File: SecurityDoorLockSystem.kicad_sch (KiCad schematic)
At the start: 12 parts, among them J1 Power In, J2 Servo, J3 RFID-RC522, J4 R307s, U1 ESP32-DEVKIT-V1, U2 L7805

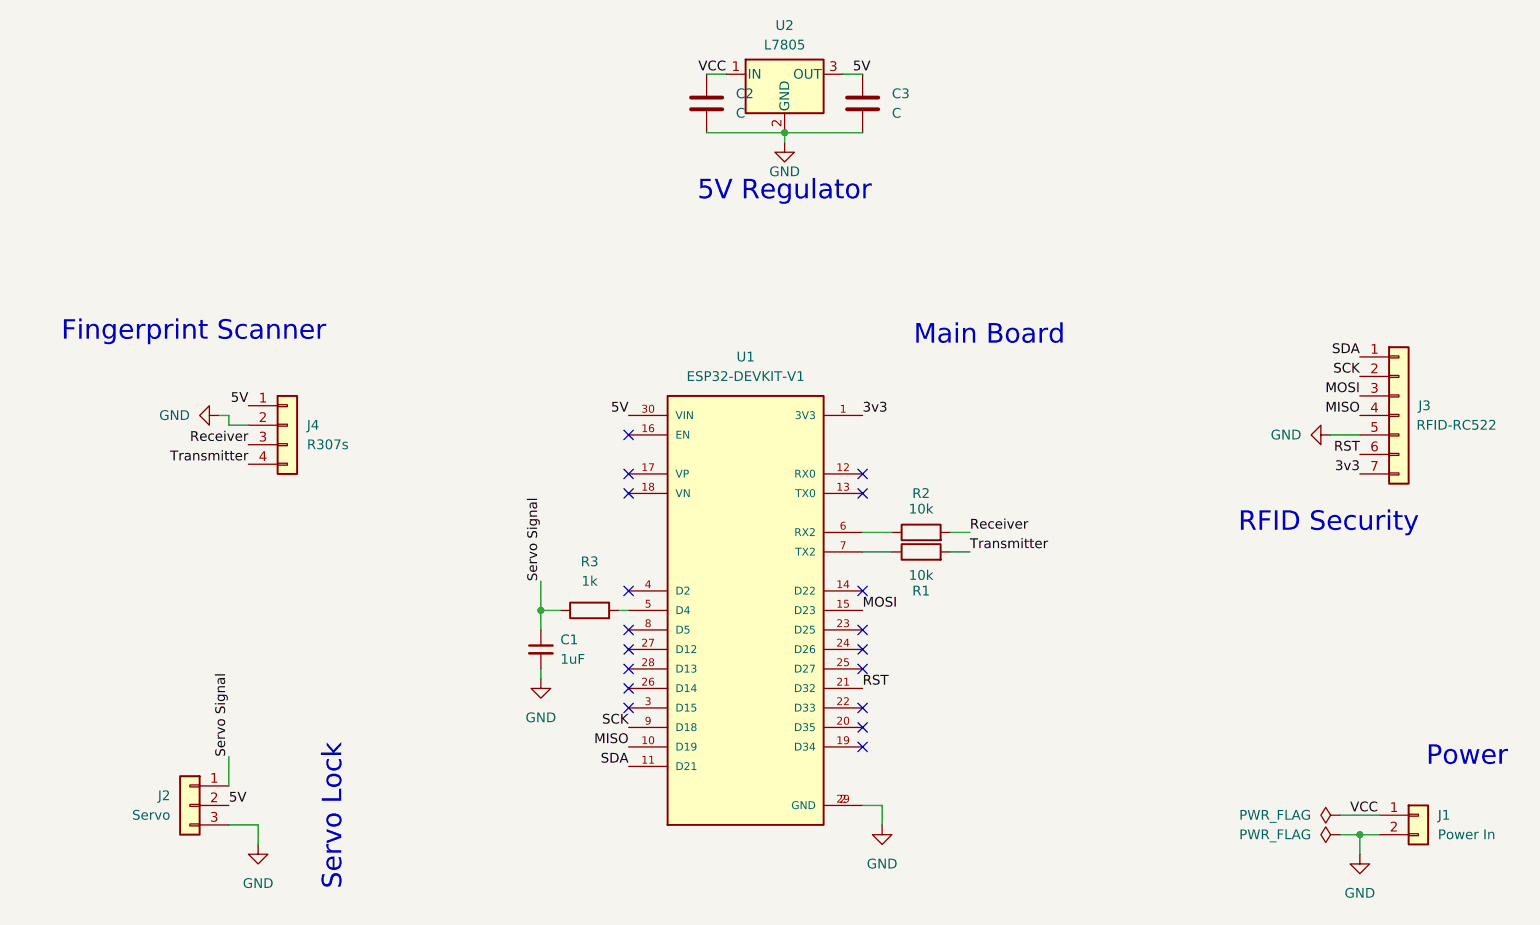
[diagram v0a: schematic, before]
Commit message: added: protection -- modified: pcb, schematic
added power source polarity protection
changed tracks (sizes and routes)
changed schematic diagram connectors to screw terminals
changed pcb connectors to screw terminals
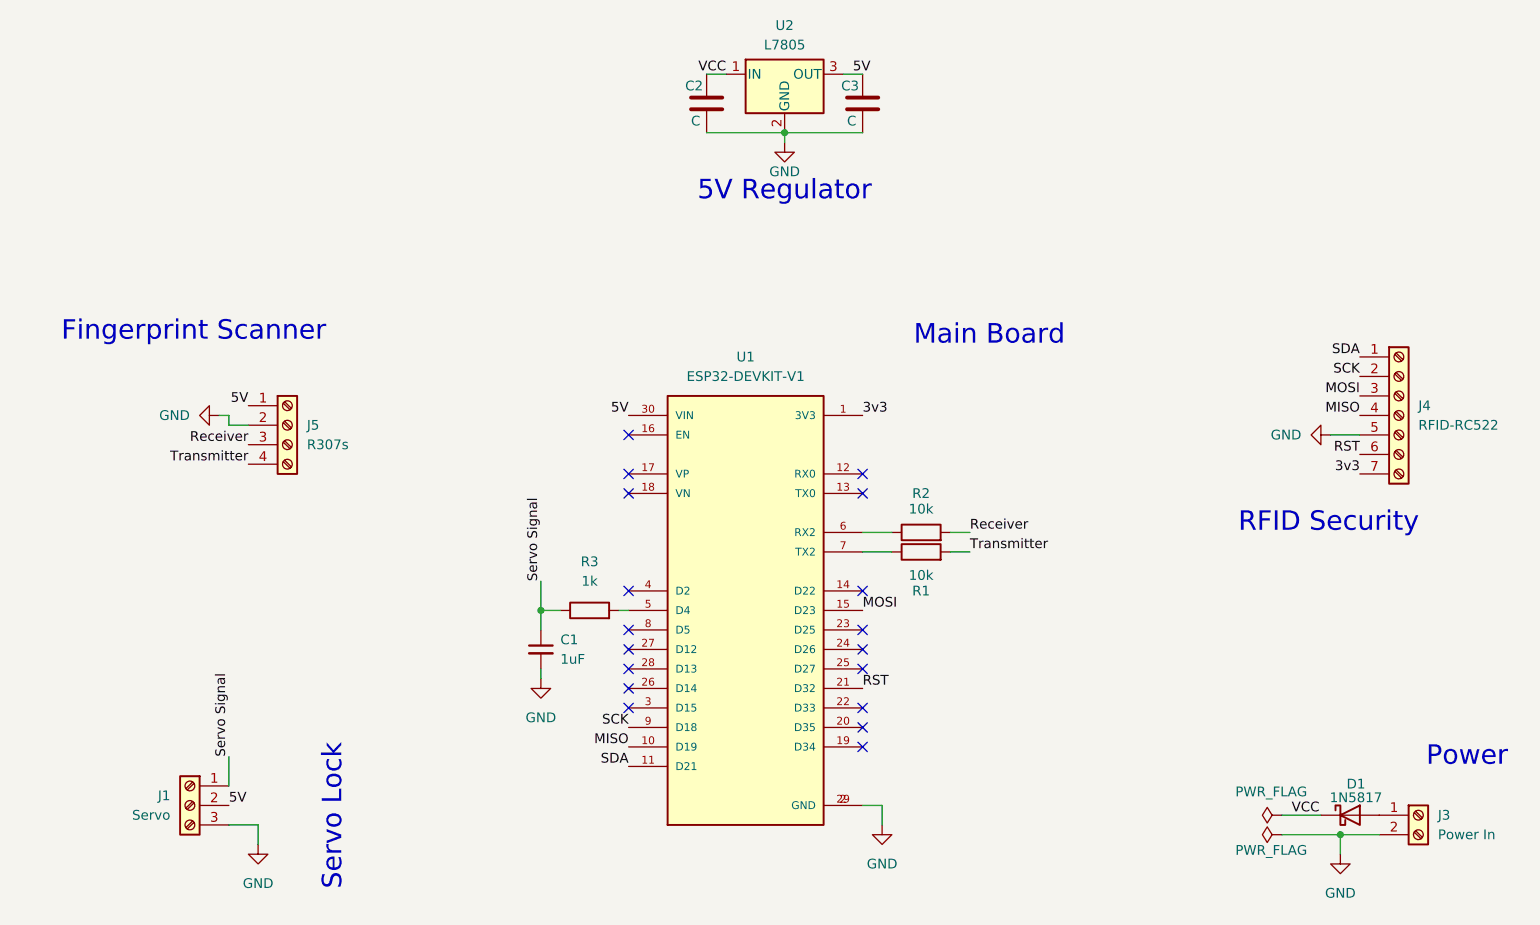
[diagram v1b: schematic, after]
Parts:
- removed J1: Power In, TerminalBlock_CUI:TerminalBlock_CUI_TB007-508-02_1x02_P5.08mm_Horizontal, symbol Connector_Generic:Conn_01x02
- removed J2: Servo, TerminalBlock_CUI:TerminalBlock_CUI_TB007-508-03_1x03_P5.08mm_Horizontal, symbol Connector_Generic:Conn_01x03
- removed J3: RFID-RC522, TerminalBlock_CUI:TerminalBlock_CUI_TB007-508-07_1x07_P5.08mm_Horizontal, symbol Connector_Generic:Conn_01x07
- removed J4: R307s, TerminalBlock_CUI:TerminalBlock_CUI_TB007-508-04_1x04_P5.08mm_Horizontal, symbol Connector_Generic:Conn_01x04
- added D1: 1N5817, Diode_THT:D_DO-41_SOD81_P7.62mm_Horizontal, symbol Diode:1N5817
- added J1: Servo, TerminalBlock_Phoenix:TerminalBlock_Phoenix_MKDS-1,5-3_1x03_P5.00mm_Horizontal, symbol Connector:Screw_Terminal_01x03
- added J3: Power In, TerminalBlock_Phoenix:TerminalBlock_Phoenix_MKDS-1,5-2_1x02_P5.00mm_Horizontal, symbol Connector:Screw_Terminal_01x02
- added J4: RFID-RC522, TerminalBlock_Phoenix:TerminalBlock_Phoenix_MKDS-1,5-7_1x07_P5.00mm_Horizontal, symbol Connector:Screw_Terminal_01x07
- added J5: R307s, TerminalBlock_Phoenix:TerminalBlock_Phoenix_MKDS-1,5-4_1x04_P5.00mm_Horizontal, symbol Connector:Screw_Terminal_01x04
- C3: footprint (none) -> Capacitor_THT:C_Radial_D5.0mm_H7.0mm_P2.00mm
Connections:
- net 3v3: now also J4.7 (Pin_7)
- net 5V: now also J1.2 (Pin_2), J5.1 (Pin_1)
- net GND: now also J1.3 (Pin_3), J3.2 (Pin_2), J4.5 (Pin_5), J5.2 (Pin_2)
- net MISO: now also J4.4 (Pin_4)
- net MOSI: now also J4.3 (Pin_3)
- net RST: now also J4.6 (Pin_6)
- net Receiver: now also J5.3 (Pin_3)
- net SCK: now also J4.2 (Pin_2)
- net SDA: now also J4.1 (Pin_1)
- net Servo Signal: now also J1.1 (Pin_1)
- net Transmitter: now also J5.4 (Pin_4)
- net VCC: now also D1.1 (K)
- new net: D1.2 (A), J3.1 (Pin_1)

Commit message: modified capacitor values
changed value of capacitors 1 and 2; C1 = 100uF, C2 = 50uF
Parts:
- C1: renamed from C2; value C -> 150uF
- C2: renamed from C3; value C -> 50uF
- renumbered C1 to C3, J4 to J1, J5 to J2, J1 to J3, J3 to J4, R2 to R1, R1 to R2, U2 to U1, U1 to U2
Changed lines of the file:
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@@
-		(polyline
-			(pts
-				(xy 125.73 33.02) (xy 125.73 59.69) (xy 160.02 59.69) (xy 160.02 33.02)
-			)
-			(stroke
-				(width 0)
-				(type dash)
-			)
-			(fill
-				(type none)
-			)
-		)
-	)
-	(rule_area
 		(polyline
 			(pts
@@
 		(polyline
 			(pts
-				(xy 104.14 72.39) (xy 180.34 72.39) (xy 180.34 151.13) (xy 104.14 151.13)
+				(xy 123.19 33.02) (xy 157.48 33.02) (xy 157.48 59.69) (xy 123.19 59.69)
 			)
 			(stroke
@@
 		)
 	)
+	(rule_area
+		(polyline
+			(pts
+				(xy 104.14 72.39) (xy 180.34 72.39) (xy 180.34 151.13) (xy 104.14 151.13)
+			)
+			(stroke
+				(width 0)
+				(type dash)
+			)
+			(fill
+				(type none)
+			)
+		)
+	)
 	(symbol
 		(lib_id "power:PWR_FLAG")
@@
 		(on_board yes)
 		(dnp no)
-		(property "Reference" "J1"
+		(property "Reference" "J3"
 			(at 60.96 135.8899 0)
 			(effects
@@
 			(project ""
 				(path "/8711d31f-b08a-48db-983d-0d74003b609c"
-					(reference "J1")
+					(reference "J3")
 					(unit 1)
 				)
@@
 		(dnp no)
 		(fields_autoplaced yes)
-		(property "Reference" "#PWR05"
+		(property "Reference" "#PWR04"
 			(at 109.22 127 0)
 			(effects
@@
 			(project "SecurityDoorLockSystem"
 				(path "/8711d31f-b08a-48db-983d-0d74003b609c"
-					(reference "#PWR05")
+					(reference "#PWR04")
 					(unit 1)
 				)
@@
 		(dnp no)
 		(fields_autoplaced yes)
-		(property "Reference" "#PWR09"
+		(property "Reference" "#PWR02"
 			(at 60.96 86.36 0)
 			(effects
@@
 			(project ""
 				(path "/8711d31f-b08a-48db-983d-0d74003b609c"
-					(reference "#PWR09")
+					(reference "#PWR02")
 					(unit 1)
 				)
@@
 		(on_board yes)
 		(dnp no)
-		(property "Reference" "R1"
+		(property "Reference" "R2"
 			(at 158.75 109.22 90)
 			(effects
@@
 			(project ""
 				(path "/8711d31f-b08a-48db-983d-0d74003b609c"
-					(reference "R1")
+					(reference "R2")
 					(unit 1)
 				)
@@
 		(dnp no)
 		(fields_autoplaced yes)
-		(property "Reference" "U2"
+		(property "Reference" "U1"
 			(at 140.97 35.56 0)
 			(effects
@@
 			(project ""
 				(path "/8711d31f-b08a-48db-983d-0d74003b609c"
-					(reference "U2")
+					(reference "U1")
 					(unit 1)
 				)
@@
 		(dnp no)
 		(fields_autoplaced yes)
-		(property "Reference" "J4"
+		(property "Reference" "J1"
 			(at 223.52 85.0899 0)
 			(effects
@@
 			(project ""
 				(path "/8711d31f-b08a-48db-983d-0d74003b609c"
-					(reference "J4")
+					(reference "J1")
 					(unit 1)
 				)
@@
 		(on_board yes)
 		(dnp no)
-		(property "Reference" "#PWR07"
+		(property "Reference" "#PWR01"
 			(at 140.97 57.15 0)
 			(effects
@@
 			(project ""
 				(path "/8711d31f-b08a-48db-983d-0d74003b609c"
-					(reference "#PWR07")
+					(reference "#PWR01")
 					(unit 1)
 				)
@@
 		(on_board yes)
 		(dnp no)
-		(property "Reference" "C3"
-			(at 148.336 43.434 0)
+		(property "Reference" "C2"
+			(at 151.384 43.434 0)
 			(effects
 				(font
@@
 			)
 		)
-		(property "Value" "C"
-			(at 149.098 48.006 0)
+		(property "Value" "50uF"
+			(at 151.638 48.006 0)
 			(effects
 				(font
@@
 			(project "SecurityDoorLockSystem"
 				(path "/8711d31f-b08a-48db-983d-0d74003b609c"
-					(reference "C3")
+					(reference "C2")
 					(unit 1)
 				)
@@
 		(dnp no)
 		(fields_autoplaced yes)
-		(property "Reference" "J5"
+		(property "Reference" "J2"
 			(at 78.74 87.6299 0)
 			(effects
@@
 			(project ""
 				(path "/8711d31f-b08a-48db-983d-0d74003b609c"
-					(reference "J5")
+					(reference "J2")
 					(unit 1)
 				)
@@
 		(dnp no)
 		(fields_autoplaced yes)
-		(property "Reference" "#PWR012"
+		(property "Reference" "#PWR03"
 			(at 205.74 88.9 0)
 			(effects
@@
 			(project ""
 				(path "/8711d31f-b08a-48db-983d-0d74003b609c"
-					(reference "#PWR012")
+					(reference "#PWR03")
 					(unit 1)
 				)
@@
 		(dnp no)
 		(fields_autoplaced yes)
-		(property "Reference" "U1"
+		(property "Reference" "U2"
 			(at 135.89 78.74 0)
 			(effects
@@
 			(project ""
 				(path "/8711d31f-b08a-48db-983d-0d74003b609c"
-					(reference "U1")
+					(reference "U2")
 					(unit 1)
 				)
@@
 		(on_board yes)
 		(dnp no)
-		(property "Reference" "R2"
+		(property "Reference" "R1"
 			(at 158.75 96.52 90)
 			(effects
@@
 			(project ""
 				(path "/8711d31f-b08a-48db-983d-0d74003b609c"
-					(reference "R2")
+					(reference "R1")
 					(unit 1)
 				)
@@
 		(dnp no)
 		(fields_autoplaced yes)
-		(property "Reference" "#PWR06"
+		(property "Reference" "#PWR07"
 			(at 213.36 149.86 0)
 			(effects
@@
 			(project ""
 				(path "/8711d31f-b08a-48db-983d-0d74003b609c"
-					(reference "#PWR06")
+					(reference "#PWR07")
 					(unit 1)
 				)
@@
 		(dnp no)
 		(fields_autoplaced yes)
-		(property "Reference" "C1"
+		(property "Reference" "C3"
 			(at 111.76 115.5762 0)
 			(effects
@@
 			(project ""
 				(path "/8711d31f-b08a-48db-983d-0d74003b609c"
-					(reference "C1")
+					(reference "C3")
 					(unit 1)
 				)
@@
 		(dnp no)
 		(fields_autoplaced yes)
-		(property "Reference" "#PWR03"
+		(property "Reference" "#PWR06"
 			(at 72.39 148.59 0)
 			(effects
@@
 			(project ""
 				(path "/8711d31f-b08a-48db-983d-0d74003b609c"
-					(reference "#PWR03")
+					(reference "#PWR06")
 					(unit 1)
 				)
@@
 		(dnp no)
 		(fields_autoplaced yes)
-		(property "Reference" "J3"
+		(property "Reference" "J4"
 			(at 226.06 138.4299 0)
 			(effects
@@
 			(project ""
 				(path "/8711d31f-b08a-48db-983d-0d74003b609c"
-					(reference "J3")
+					(reference "J4")
 					(unit 1)
 				)
@@
 		(dnp no)
 		(fields_autoplaced yes)
-		(property "Reference" "#PWR02"
+		(property "Reference" "#PWR05"
 			(at 153.67 146.05 0)
 			(effects
@@
 			(project ""
 				(path "/8711d31f-b08a-48db-983d-0d74003b609c"
-					(reference "#PWR02")
+					(reference "#PWR05")
 					(unit 1)
 				)
@@
 		(on_board yes)
 		(dnp no)
-		(property "Reference" "C2"
+		(property "Reference" "C1"
 			(at 128.016 43.434 0)
 			(effects
@@
 			)
 		)
-		(property "Value" "C"
-			(at 128.778 48.006 0)
+		(property "Value" "150uF"
+			(at 124.714 48.006 0)
 			(effects
 				(font
@@
 			(project ""
 				(path "/8711d31f-b08a-48db-983d-0d74003b609c"
-					(reference "C2")
-					(unit 1)
-				)
+					(reference "C1")
+					(unit 1)
+				)

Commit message: added lcd
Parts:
- added J5: LCD Conn, TerminalBlock_Phoenix:TerminalBlock_Phoenix_MKDS-1,5-4_1x04_P5.00mm_Horizontal, symbol Connector:Screw_Terminal_01x04
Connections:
- net 5V: now also J5.2 (Pin_2)
- net GND: now also J5.1 (Pin_1)
- net SDA: now also J5.4 (Pin_4); no longer J1.1 (Pin_1)
- net Rx: now reaches U2.12 (RX0)
- net Rx: now also J1.1 (Pin_1)
- net Tx: now reaches U2.13 (TX0)
- net Tx: now also J1.4 (Pin_4)
- net SCL: now reaches U2.14 (D22)
- net SCL: now also J5.3 (Pin_3)
- net MISO: no longer names the net of U2.10 (D19)
- net MISO: no longer J1.4 (Pin_4)
- no-connect marks 18 -> 16
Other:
- note added: "Display"
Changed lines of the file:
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@@
+		)
+	)
+	(text "Display\n"
+		(exclude_from_sim no)
+		(at 213.868 56.134 0)
+		(effects
+			(font
+				(size 2.54 2.54)
+			)
 		)
 	)
@@
 	)
 	(no_connect
-		(at 151.13 109.22)
-	)
-	(no_connect
 		(at 151.13 116.84)
 	)
@@
 	)
 	(no_connect
-		(at 151.13 96.52)
-	)
-	(no_connect
 		(at 120.65 96.52)
 	)
@@
 	)
 	(no_connect
+		(at 120.65 129.54)
+	)
+	(no_connect
 		(at 120.65 124.46)
 	)
@@
 		(at 120.65 119.38)
 	)
-	(no_connect
-		(at 151.13 93.98)
-	)
 	(wire
 		(pts
@@
 		(pts
 			(xy 213.36 143.51) (xy 213.36 140.97)
+		)
+		(stroke
+			(width 0)
+			(type default)
+		)
+	)
+	(wire
+		(pts
+			(xy 203.2 44.45) (xy 209.55 44.45)
 		)
 		(stroke
@@
 		)
 	)
+	(label "Rx"
+		(at 151.13 93.98 0)
+		(effects
+			(font
+				(size 1.27 1.27)
+			)
+			(justify left bottom)
+		)
+	)
 	(label "RST"
 		(at 151.13 121.92 0)
@@
 		)
 	)
+	(label "5V"
+		(at 209.55 46.99 180)
+		(effects
+			(font
+				(size 1.27 1.27)
+			)
+			(justify right bottom)
+		)
+	)
 	(label "SDA"
 		(at 120.65 132.08 180)
@@
 		)
 	)
-	(label "SDA"
+	(label "Rx"
 		(at 215.9 78.74 180)
 		(effects
@@
 		)
 	)
+	(label "SDA"
+		(at 209.55 52.07 180)
+		(effects
+			(font
+				(size 1.27 1.27)
+			)
+			(justify right bottom)
+		)
+	)
 	(label "VCC"
 		(at 133.35 41.91 180)
@@
 		)
 	)
-	(label "MISO"
+	(label "Tx"
 		(at 215.9 86.36 180)
 		(effects
@@
 		)
 	)
+	(label "SCL"
+		(at 151.13 109.22 0)
+		(effects
+			(font
+				(size 1.27 1.27)
+			)
+			(justify left bottom)
+		)
+	)
 	(label "3v3"
 		(at 151.13 86.36 0)
@@
 		)
 	)
+	(label "Tx"
+		(at 151.13 96.52 0)
+		(effects
+			(font
+				(size 1.27 1.27)
+			)
+			(justify left bottom)
+		)
+	)
 	(label "3v3"
 		(at 215.9 93.98 180)
@@
 		)
 	)
-	(label "MISO"
-		(at 120.65 129.54 180)
+	(label "SCL"
+		(at 209.55 49.53 180)
 		(effects
 			(font
@@
 			(pts
 				(xy 53.34 111.76) (xy 53.34 151.13) (xy 86.36 151.13) (xy 86.36 111.76)
+			)
+			(stroke
+				(width 0)
+				(type dash)
+			)
+			(fill
+				(type none)
+			)
+		)
+	)
+	(rule_area
+		(polyline
+			(pts
+				(xy 200.66 41.91) (xy 200.66 58.42) (xy 227.33 58.42) (xy 227.33 41.91)
 			)
 			(stroke
@@
 	)
 	(symbol
+		(lib_id "power:GND")
+		(at 203.2 44.45 0)
+		(unit 1)
+		(exclude_from_sim no)
+		(in_bom yes)
+		(on_board yes)
+		(dnp no)
+		(fields_autoplaced yes)
+		(property "Reference" "#PWR08"
+			(at 203.2 50.8 0)
+			(effects
+				(font
+					(size 1.27 1.27)
+				)
+				(hide yes)
+			)
+		)
+		(property "Value" "GND"
+			(at 203.2 49.53 0)
+			(effects
+				(font
+					(size 1.27 1.27)
+				)
+			)
+		)
+		(property "Footprint" ""
+			(at 203.2 44.45 0)
+			(effects
+				(font
+					(size 1.27 1.27)
+				)
+				(hide yes)
+			)
+		)
+		(property "Datasheet" ""
+			(at 203.2 44.45 0)
+			(effects
+				(font
+					(size 1.27 1.27)
+				)
+				(hide yes)
+			)
+		)
+		(property "Description" "Power symbol creates a global label with name \"GND\" , ground"
+			(at 203.2 44.45 0)
+			(effects
+				(font
+					(size 1.27 1.27)
+				)
+				(hide yes)
+			)
+		)
+		(pin "1"
+		)
+		(instances
+			(project ""
+				(path "/8711d31f-b08a-48db-983d-0d74003b609c"
+					(reference "#PWR08")
+					(unit 1)
+				)
+			)
+		)
+	)
+	(symbol
 		(lib_id "Device:C_Small")
 		(at 109.22 116.84 0)
@@
 					(unit 1)
 				)
+			)
+		)
+	)
+	(symbol
+		(lib_id "Connector:Screw_Terminal_01x04")
+		(at 214.63 46.99 0)
+		(unit 1)
+		(exclude_from_sim no)
+		(in_bom yes)
+		(on_board yes)
+		(dnp no)
+		(fields_autoplaced yes)
+		(property "Reference" "J5"
+			(at 217.17 46.9899 0)
+			(effects
+				(font
+					(size 1.27 1.27)
+				)
+				(justify left)
+			)
+		)
+		(property "Value" "LCD Conn"
+			(at 217.17 49.5299 0)
+			(effects
+				(font
+					(size 1.27 1.27)
+				)
+				(justify left)
+			)
+		)
+		(property "Footprint" "TerminalBlock_Phoenix:TerminalBlock_Phoenix_MKDS-1,5-4_1x04_P5.00mm_Horizontal"
+			(at 214.63 46.99 0)
+			(effects
+				(font
+					(size 1.27 1.27)
+				)
+				(hide yes)
+			)
+		)
+		(property "Datasheet" "~"
+			(at 214.63 46.99 0)
+			(effects
+				(font
+					(size 1.27 1.27)
+				)
+				(hide yes)
+			)
+		)
+		(property "Description" "Generic screw terminal, single row, 01x04, script generated (kicad-library-utils/schlib/autogen/connector/)"
+			(at 214.63 46.99 0)
+			(effects
+				(font
+					(size 1.27 1.27)
+				)
+				(hide yes)
+			)
+		)
+		(pin "4"
+		)
+		(pin "3"
+		)
+		(pin "2"
+		)
+		(pin "1"
+		)
+		(instances
+			(project ""
+				(path "/8711d31f-b08a-48db-983d-0d74003b609c"
+					(reference "J5")
+					(unit 1)
+				)
